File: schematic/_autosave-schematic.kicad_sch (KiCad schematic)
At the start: 32 parts, among them IC2 AS312, J3 USB_C_Receptacle_USB2.0, SW2 SW_Push, SW3 SW_Push, U1 ESP32-S3-WROOM-1, U3 AM2302

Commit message: more Routing
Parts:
- renumbered Switch+ to Switch+1, Switch- to Switch-1
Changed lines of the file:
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@@
 		(on_board yes)
 		(dnp no)
-		(property "Reference" "Switch-"
+		(property "Reference" "Switch-1"
 			(at 271.78 147.828 0)
 			(effects
@@
 			(project "schematic"
 				(path "/374f5031-bd65-4a4b-92ce-befdd0c9f08b"
-					(reference "Switch-")
+					(reference "Switch-1")
 					(unit 1)
 				)
@@
 		(on_board yes)
 		(dnp no)
-		(property "Reference" "Switch+"
+		(property "Reference" "Switch+1"
 			(at 256.54 149.098 0)
 			(effects
@@
 			(project "schematic"
 				(path "/374f5031-bd65-4a4b-92ce-befdd0c9f08b"
-					(reference "Switch+")
-					(unit 1)
-				)
+					(reference "Switch+1")
+					(unit 1)
+				)

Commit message: more Routing
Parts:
- added +5V1: 5v, TestPoint:TestPoint_Loop_D2.50mm_Drill1.85mm, symbol Connector:TestPoint
- added GND1: GND, TestPoint:TestPoint_Loop_D2.50mm_Drill1.85mm, symbol Connector:TestPoint
- renumbered SW3 to BOOT1, SW2 to RESET1
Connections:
- net +5V: now also +5V1.1
- net GND: now also GND1.1
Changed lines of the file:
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@@
 	)
 	(junction
+		(at 168.91 32.385)
+		(diameter 0)
+		(color 0 0 0 0)
+	)
+	(junction
 		(at 46.355 41.91)
 		(diameter 0)
@@
 	)
 	(junction
+		(at 169.545 21.59)
+		(diameter 0)
+		(color 0 0 0 0)
+	)
+	(junction
 		(at 54.61 36.83)
 		(diameter 0)
@@
 	(wire
 		(pts
+			(xy 168.91 21.59) (xy 169.545 21.59)
+		)
+		(stroke
+			(width 0)
+			(type default)
+		)
+	)
+	(wire
+		(pts
 			(xy 107.95 30.48) (xy 107.95 43.815)
 		)
@@
 	(wire
 		(pts
+			(xy 168.91 32.385) (xy 168.91 34.29)
+		)
+		(stroke
+			(width 0)
+			(type default)
+		)
+	)
+	(wire
+		(pts
 			(xy 88.9 29.845) (xy 88.9 27.94)
 		)
@@
 	(wire
 		(pts
-			(xy 168.91 21.59) (xy 169.545 21.59)
-		)
-		(stroke
-			(width 0)
-			(type default)
-		)
-	)
-	(wire
-		(pts
 			(xy 139.7 30.48) (xy 139.7 32.385)
 		)
@@
 	(wire
 		(pts
+			(xy 181.61 34.29) (xy 168.91 34.29)
+		)
+		(stroke
+			(width 0)
+			(type default)
+		)
+	)
+	(wire
+		(pts
 			(xy 292.1 95.25) (xy 288.29 95.25)
 		)
@@
 	(wire
 		(pts
+			(xy 169.545 21.59) (xy 182.88 21.59)
+		)
+		(stroke
+			(width 0)
+			(type default)
+		)
+	)
+	(wire
+		(pts
 			(xy 237.49 105.41) (xy 227.33 105.41)
 		)
@@
 	)
 	(label "+3V3"
-		(at 118.237 74.93 180)
+		(at 116.84 74.93 180)
 		(effects
 			(font
@@
 	)
 	(symbol
+		(lib_id "Connector:TestPoint")
+		(at 181.61 34.29 270)
+		(unit 1)
+		(exclude_from_sim no)
+		(in_bom yes)
+		(on_board yes)
+		(dnp no)
+		(property "Reference" "GND1"
+			(at 186.182 36.83 0)
+			(effects
+				(font
+					(size 1.27 1.27)
+				)
+				(justify left)
+			)
+		)
+		(property "Value" "GND"
+			(at 183.642 36.83 0)
+			(effects
+				(font
+					(size 1.27 1.27)
+				)
+				(justify left)
+			)
+		)
+		(property "Footprint" "TestPoint:TestPoint_Loop_D2.50mm_Drill1.85mm"
+			(at 181.61 39.37 0)
+			(effects
+				(font
+					(size 1.27 1.27)
+				)
+				(hide yes)
+			)
+		)
+		(property "Datasheet" "~"
+			(at 181.61 39.37 0)
+			(effects
+				(font
+					(size 1.27 1.27)
+				)
+				(hide yes)
+			)
+		)
+		(property "Description" ""
+			(at 181.61 34.29 0)
+			(effects
+				(font
+					(size 1.27 1.27)
+				)
+				(hide yes)
+			)
+		)
+		(pin "1"
+		)
+		(instances
+			(project "schematic"
+				(path "/374f5031-bd65-4a4b-92ce-befdd0c9f08b"
+					(reference "GND1")
+					(unit 1)
+				)
+			)
+		)
+	)
+	(symbol
 		(lib_id "AS312:AS312")
 		(at 247.65 105.41 0)
@@
 		(dnp no)
 		(fields_autoplaced yes)
-		(property "Reference" "SW2"
+		(property "Reference" "RESET1"
 			(at 27.94 88.9 0)
 			(effects
@@
 			(project "schematic"
 				(path "/374f5031-bd65-4a4b-92ce-befdd0c9f08b"
-					(reference "SW2")
+					(reference "RESET1")
 					(unit 1)
 				)
@@
 	)
 	(symbol
+		(lib_id "Connector:TestPoint")
+		(at 182.88 21.59 270)
+		(unit 1)
+		(exclude_from_sim no)
+		(in_bom yes)
+		(on_board yes)
+		(dnp no)
+		(property "Reference" "+5V1"
+			(at 187.452 24.13 0)
+			(effects
+				(font
+					(size 1.27 1.27)
+				)
+				(justify left)
+			)
+		)
+		(property "Value" "5v"
+			(at 184.912 24.13 0)
+			(effects
+				(font
+					(size 1.27 1.27)
+				)
+				(justify left)
+			)
+		)
+		(property "Footprint" "TestPoint:TestPoint_Loop_D2.50mm_Drill1.85mm"
+			(at 182.88 26.67 0)
+			(effects
+				(font
+					(size 1.27 1.27)
+				)
+				(hide yes)
+			)
+		)
+		(property "Datasheet" "~"
+			(at 182.88 26.67 0)
+			(effects
+				(font
+					(size 1.27 1.27)
+				)
+				(hide yes)
+			)
+		)
+		(property "Description" ""
+			(at 182.88 21.59 0)
+			(effects
+				(font
+					(size 1.27 1.27)
+				)
+				(hide yes)
+			)
+		)
+		(pin "1"
+		)
+		(instances
+			(project "schematic"
+				(path "/374f5031-bd65-4a4b-92ce-befdd0c9f08b"
+					(reference "+5V1")
+					(unit 1)
+				)
+			)
+		)
+	)
+	(symbol
 		(lib_id "Device:C_Small")
 		(at 250.19 54.61 90)
@@
 		(dnp no)
 		(fields_autoplaced yes)
-		(property "Reference" "SW3"
+		(property "Reference" "BOOT1"
 			(at 31.115 127.635 0)
 			(effects
@@
 			(project "schematic"
 				(path "/374f5031-bd65-4a4b-92ce-befdd0c9f08b"
-					(reference "SW3")
+					(reference "BOOT1")
 					(unit 1)
 				)

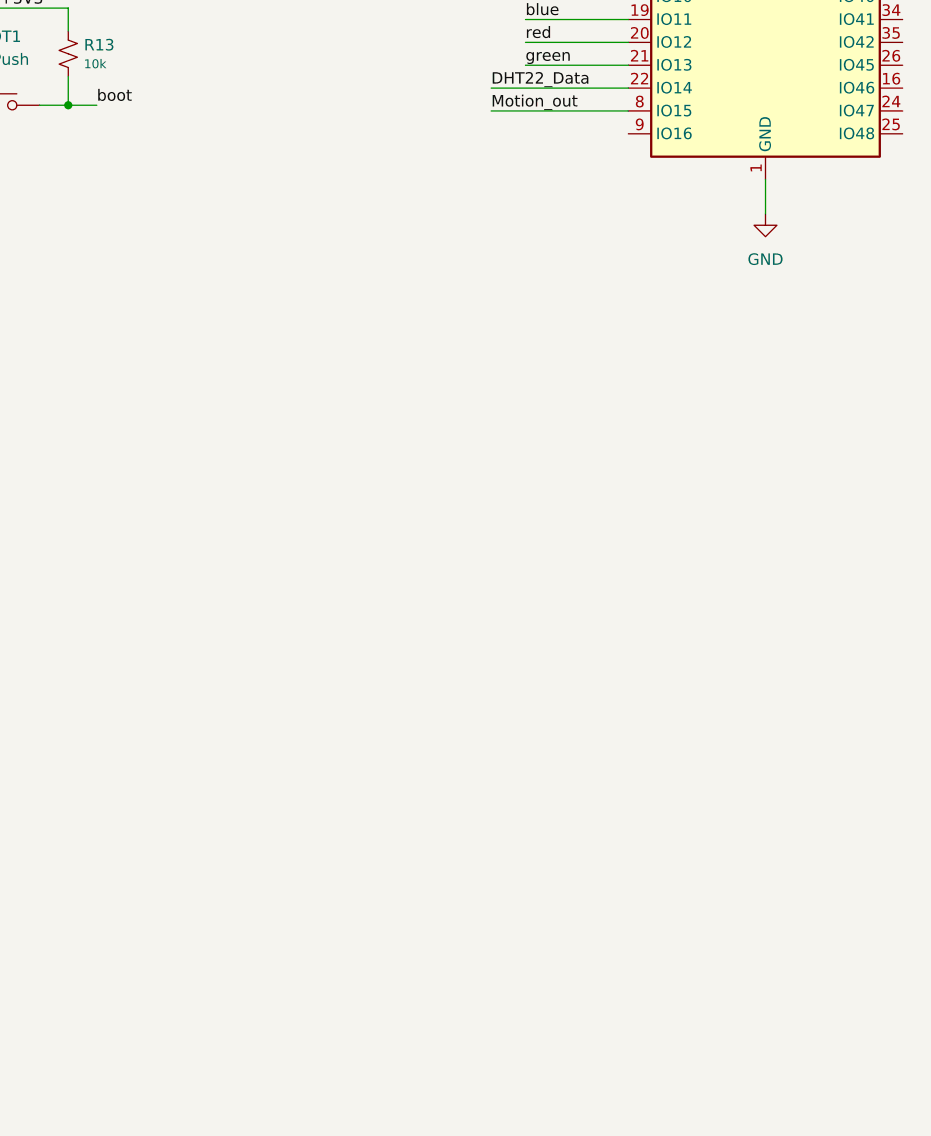
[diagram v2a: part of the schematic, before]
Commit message: changinge mcu and shift level
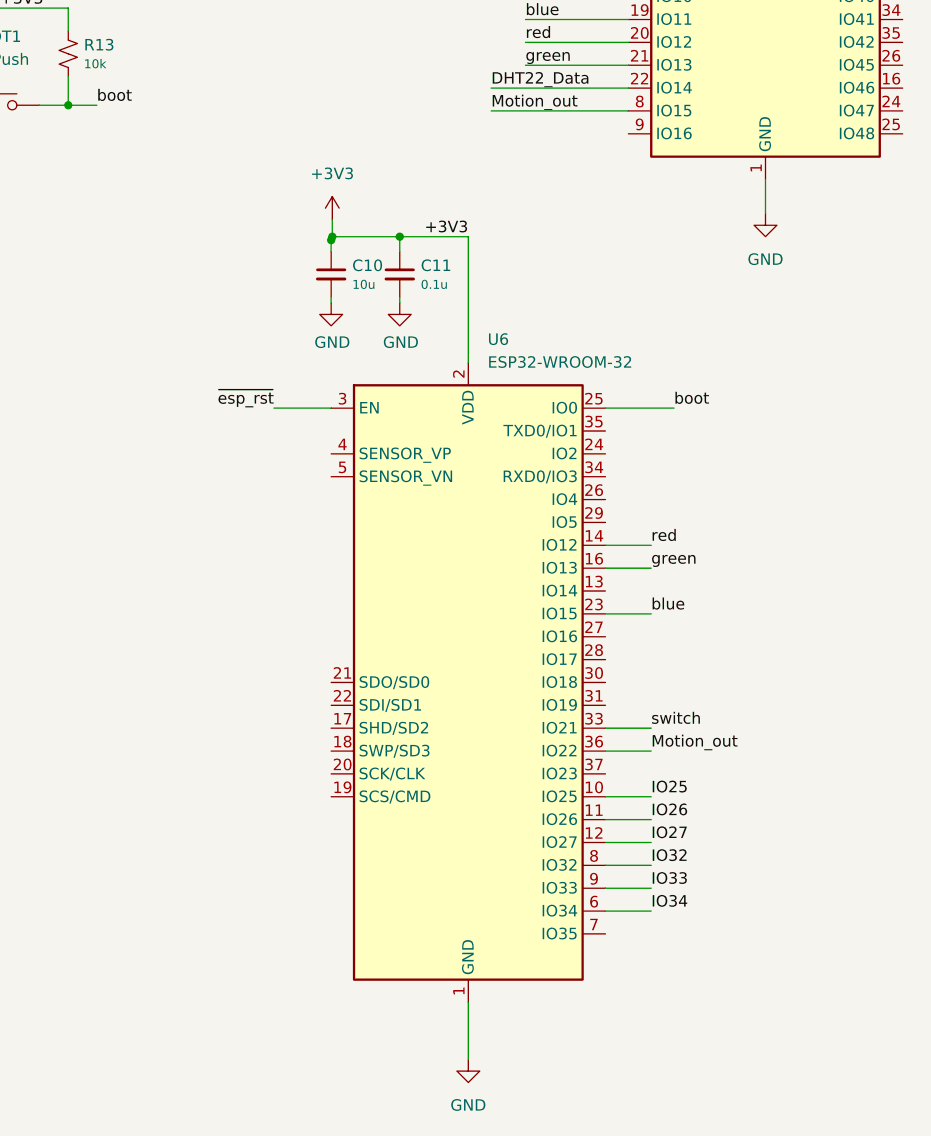
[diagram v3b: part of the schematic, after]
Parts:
- added C10: 10u, Capacitor_SMD:C_0402_1005Metric, symbol Device:C_Small
- added C11: 0.1u, Capacitor_SMD:C_0402_1005Metric, symbol Device:C_Small
- added U6: ESP32-WROOM-32, RF_Module:ESP32-WROOM-32, symbol RF_Module:ESP32-WROOM-32
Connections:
- net +3V3: now also C10.1, C11.1, U6.2 (VDD)
- net GND: now also C10.2, C11.2, U6.1 (GND), U6.15 (GND), U6.38 (GND), U6.39 (GND)
- net Motion_out: now also U6.36 (IO22)
- net blue: now also U6.23 (IO15)
- net boot: now also U6.25 (IO0)
- net green: now also U6.16 (IO13)
- net red: now also U6.14 (IO12)
- net switch: now also U6.33 (IO21)
- net ~{esp_rst}: now also U6.3 (EN)
- new net IO25: U6.10 (IO25)
- new net IO26: U6.11 (IO26)
- new net IO27: U6.12 (IO27)
- new net IO32: U6.8 (IO32)
- new net IO33: U6.9 (IO33)
- new net IO34: U6.6 (IO34)

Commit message: changinge mcu and shift level
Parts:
- removed C4: 10u, Capacitor_SMD:C_0402_1005Metric, symbol Device:C_Small
- removed C5: 0.1u, Capacitor_SMD:C_0402_1005Metric, symbol Device:C_Small
- removed U1: ESP32-S3-WROOM-1, RF_Module:ESP32-S3-WROOM-1, symbol RF_Module:ESP32-S3-WROOM-1
- added C13: 22uF, Capacitor_SMD:C_0402_1005Metric, symbol Device:C_Small
- added C14: 100nF, Capacitor_SMD:C_0402_1005Metric, symbol Device:C_Small
- added C15, C16: 22pF, Capacitor_SMD:C_0402_1005Metric, symbol Device:C_Small
- added D10, D11, D12: B5819W, Diode_SMD:D_SOD-123, symbol Device:D_Schottky_Small
- added D13: BAT54C, Package_TO_SOT_SMD:SOT-23, symbol Diode:BAT54C
- added Q10, Q11: MMBT3904, Package_TO_SOT_SMD:SOT-23, symbol Transistor_BJT:MMBT3904
- added R11, R19, R20, R21: 10k, Resistor_SMD:R_0402_1005Metric, symbol Device:R_Small_US
- added R22: 220R, Resistor_SMD:R_0402_1005Metric, symbol Device:R_Small_US
- added U8: CH340T(SSOP20W), Package_SO:SSOP-20_5.3x7.2mm_P0.65mm, symbol GCL_Integrated-Circuits:CH340T(SSOP20W)
- added Y1: 12MHz, Crystal:Crystal_SMD_2520-4Pin_2.5x2.0mm, symbol Device:Crystal_GND2_Small
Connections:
- net +5V: now also C13.1, R11.1, U8.19 (VCC)
- net D+: now also U8.6 (UD+)
- net D-: now also U8.7 (UD-)
- net DHT22_Data: now also U6.31 (IO19)
- net ESP_RX: now also U6.34 (RXD0/IO3), D10.2 (A), R19.2
- net ESP_TX: now also U6.35 (TXD0/IO1), D11.1 (K)
- net GND: now also C13.2, C14.2, C15.2, C16.2, U8.8 (GND), Y1.2
- net boot: now also D13.2
- net ~{esp_rst}: now also D12.2 (A)
- net IO2: now reaches U6.24 (IO2)
- net IO2: now also D13.1
- net IO4: now reaches U6.26 (IO4)
- new net: C16.1, U8.10 (XO), Y1.3
- new net: D10.1 (K), U8.3 (TXD)
- new net: D11.2 (A), R11.2, U8.4 (RXD)
- new net: C14.1, R19.1, U8.5 (V3)
- new net: C15.1, U8.9 (XI), Y1.1
- new net: Q10.1 (B), R20.1
- new net: D12.1 (K), Q10.3 (C)
- new net: D13.3, R22.1
- new net: Q11.3 (C), R22.2
- new net: Q11.1 (B), R21.1
- new net dtr: Q10.2 (E), Q11.2 (E), R20.2, R21.2, U8.15 (DTR#), U8.16 (RTS#)
- no-connect marks 2 -> 8
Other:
- note added: "0"
- note added: "1"
- note added: "Auto Reset Circuit"
- note added: "Auto program"
- note added: "DTR RTS->EN IO0"
- moved on the sheet: C10, C11, U6
